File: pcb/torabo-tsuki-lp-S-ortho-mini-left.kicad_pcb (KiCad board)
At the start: 2 copper layers, 138.8 x 74 mm, 72 parts, among them J101 Conn_01x06_MountingPin, SW10 SW_Push, SW101 SW_SPDT, SW11 SW_Push, SW12 SW_Push, SW13 SW_Push, SW15 SW_Push, SW16 SW_Push, SW17 SW_Push, SW18 SW_Push, SW19 SW_Push, SW20 SW_Push, SW22 SW_Push, SW23 SW_Push, SW24 SW_Push, SW25 SW_Push, SW26 SW_Push, SW27 SW_Push, SW28 SW_Push, SW29 SW_Push, SW30 SW_Push, SW31 SW_Push, SW32 SW_Push, SW33 SW_Push, SW34 SW_Push, SW35 SW_Push, SW8 SW_Push, SW9 SW_Push, U101 XIAO nRF52840 Plus, U102 XCL103D503CR-G, U103 XC8111AA01MR-G

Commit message: Rename PCB silkscreen to kb-1
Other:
- board text added: "kb-1"
- board text removed: "torabo-tsuki om(s) v0"
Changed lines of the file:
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@@
 		)
 	)
-	(gr_text "torabo-tsuki om(s) v0"
+	(gr_text "kb-1"
 		(at 114 75.8 0)
 		(layer "F.SilkS")

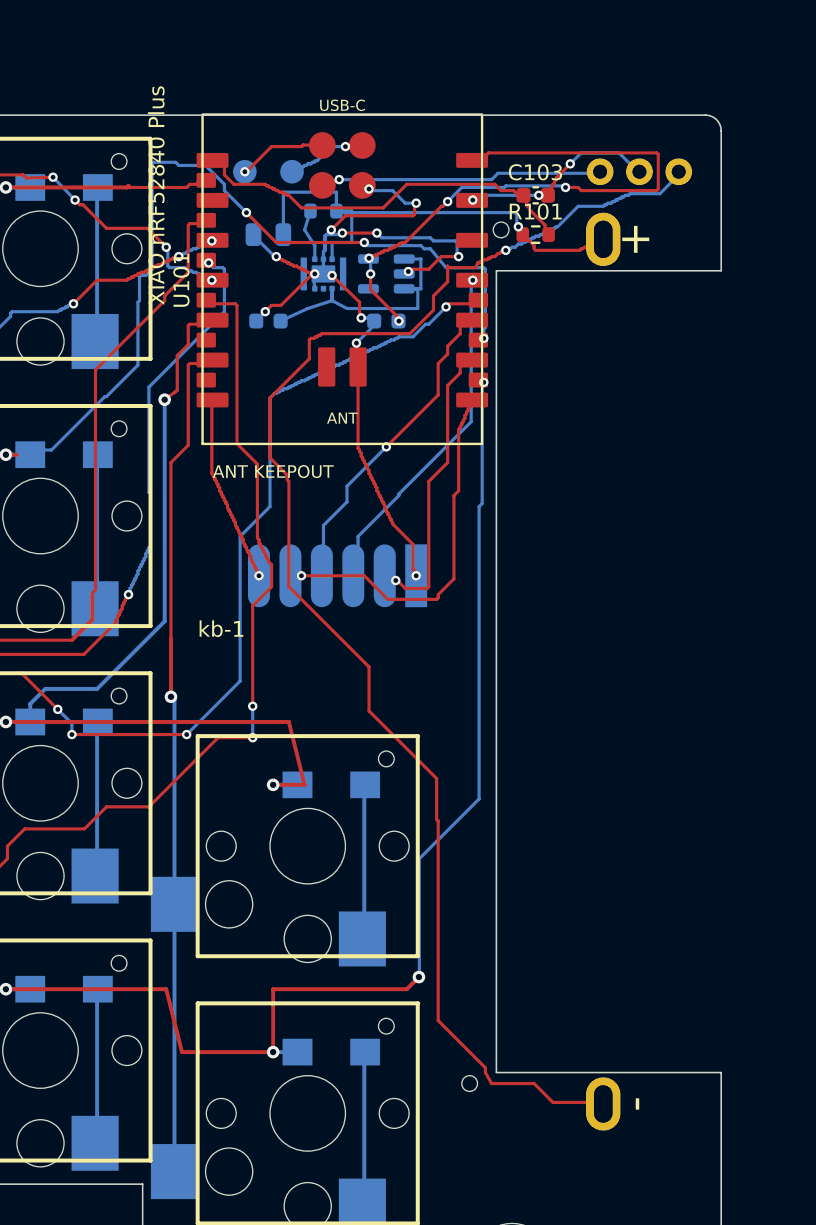
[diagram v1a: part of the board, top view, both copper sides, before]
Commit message: WIP: checkpoint single-XIAO PCB and vertical PHD conversion
Preserve the current single-controller PCB, schematics, documentation, and manufacturing artifacts. Include the vertical PHD placement/routing experiment; its candidate boards still fail DRC and are not production-ready.
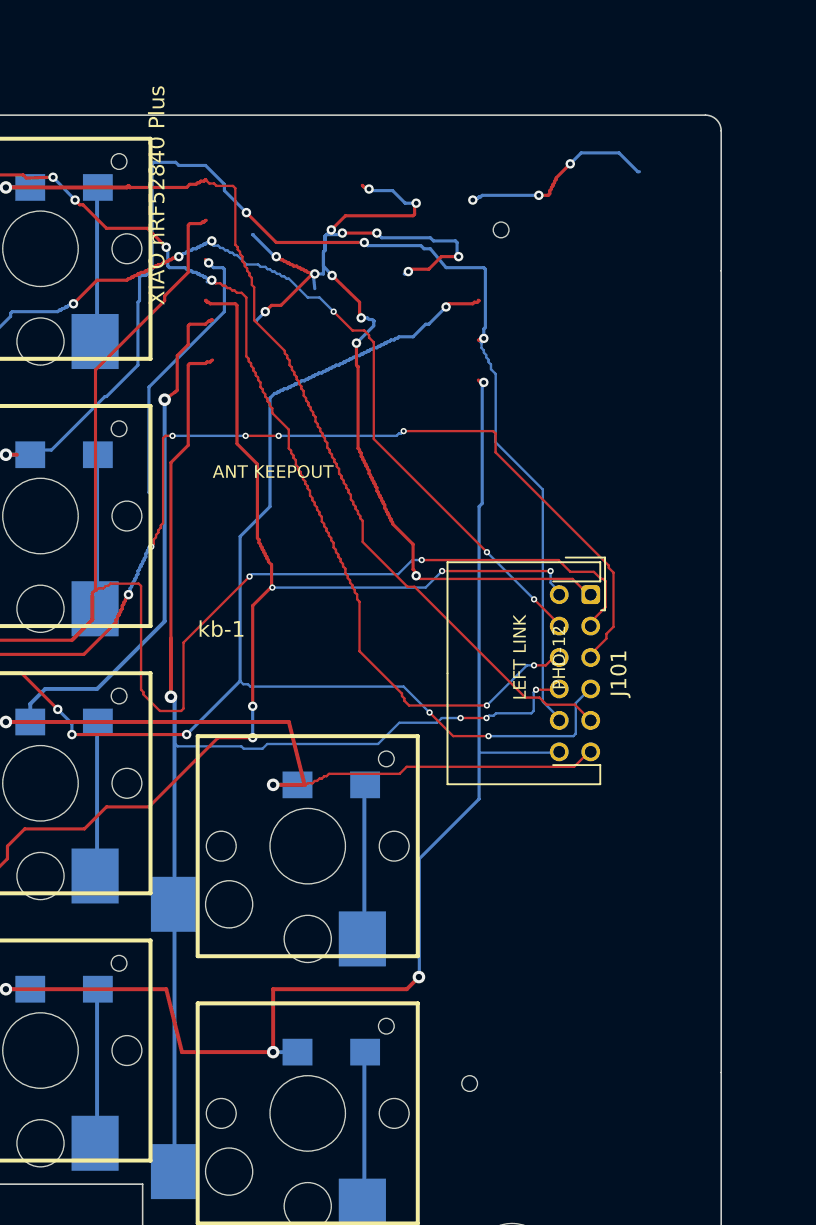
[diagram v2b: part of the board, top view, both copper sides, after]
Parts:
- removed BT101: GB-BH-4X1-WP, Library:battery_holder_AAA_1x_P55mm
- removed C101: 10uF 25V X5R, C_0805_2012Metric
- removed C102: 10uF 16V X5R, C_0603_1608Metric
- removed C103, C104: 0.1uF 50V X7R, C_0603_1608Metric
- removed R101: 10k, R_0603_1608Metric
- removed R102: 100k, R_0603_1608Metric
- removed SW101: SW_SPDT, Library:ISH-1260-HA-G
- removed TP101: SWDIO, TestPoint_Pad_D1.5mm
- removed TP102: SWDCLK, TestPoint_Pad_D1.5mm
- removed U101: XIAO nRF52840 Plus, XIAO-nRF52840-Plus-SMD
- removed U102: XCL103D503CR-G, CL-2025-02
- removed U103: XC8111AA01MR-G, SOT-23-5
- J101: value Conn_01x06_MountingPin -> S12B-PHDSS; footprint Library:ffc-6p-adapter -> Connector_JST:JST_PHD_S12B-PHDSS_2x06_P2.00mm_Horizontal; moved to F.Cu
- moved J101 16.1 mm to (139.0, 73.0), turned to -90 degrees
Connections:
- D10 pad 2: /left/ROW1 -> /left/LROW0
- D11 pad 2: /left/ROW1 -> /left/LROW0
- D12 pad 2: /left/ROW1 -> /left/LROW0
- D13 pad 2: /left/ROW1 -> /left/LROW0
- D15 pad 2: /left/ROW2 -> /left/LROW1
- D16 pad 2: /left/ROW2 -> /left/LROW1
- D17 pad 2: /left/ROW2 -> /left/LROW1
- D18 pad 2: /left/ROW2 -> /left/LROW1
- D19 pad 2: /left/ROW2 -> /left/LROW1
- D20 pad 2: /left/ROW2 -> /left/LROW1
- D22 pad 2: /left/ROW3 -> /left/LROW2
- D23 pad 2: /left/ROW3 -> /left/LROW2
- D24 pad 2: /left/ROW3 -> /left/LROW2
- D25 pad 2: /left/ROW3 -> /left/LROW2
- D26 pad 2: /left/ROW3 -> /left/LROW2
- D27 pad 2: /left/ROW3 -> /left/LROW2
- D28 pad 2: /left/ROW3 -> /left/LROW2
- D29 pad 2: /left/ROW4 -> /left/LROW3
- D30 pad 2: /left/ROW4 -> /left/LROW3
- D31 pad 2: /left/ROW4 -> /left/LROW3
- D32 pad 2: /left/ROW4 -> /left/LROW3
- D33 pad 2: /left/ROW4 -> /left/LROW3
- D34 pad 2: /left/ROW4 -> /left/LROW3
- D35 pad 2: /left/ROW4 -> /left/LROW3
- D8 pad 2: /left/ROW1 -> /left/LROW0
- D9 pad 2: /left/ROW1 -> /left/LROW0
- J101 pad 2: /left/SCLK -> /left/COL0
- J101 pad 3: /left/SDIO -> /left/COL1
- J101 pad 4: /left/MOTION -> /left/COL2
- J101 pad 5: /left/CS -> /left/COL3
- J101 pad 6: VCC -> /left/COL4
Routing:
- net /left/LROW3: track 0.00 -> 180.3 mm, vias 0 -> 9
- net /left/LROW1: track 0.00 -> 178.8 mm, vias 0 -> 9
- net /left/LROW2: track 0.00 -> 177.8 mm, vias 0 -> 8
- net /left/ROW4: track 175.1 -> 0.00 mm, vias 9 -> 0
- net /left/LROW0: track 0.00 -> 160.2 mm, vias 0 -> 6
- net /left/ROW3: track 158.7 -> 0.00 mm, vias 8 -> 0
- net /left/ROW2: track 152.4 -> 0.00 mm, vias 9 -> 0
- net /left/ROW1: track 113.0 -> 0.00 mm, vias 6 -> 0
- net Net-(BT101--): track 91.1 -> 0.00 mm, vias 1 -> 0
- net /left/COL1: track 170.8 -> 221.0 mm, vias 1 -> 3
- net /left/COL3: track 128.6 -> 175.3 mm, vias 3 -> 8
- net /left/COL4: track 97.3 -> 141.0 mm, vias 6 -> 8
- net /left/SYS_5V: track 39.7 -> 0.00 mm, vias 5 -> 0
- net /left/COL2: track 134.9 -> 171.0 mm, vias 5 -> 8
- net +BATT: track 31.6 -> 0.00 mm, vias 1 -> 0
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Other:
- outline, holes or cut-outs redrawn
- board text added: "LEFT LINK"
- board text added: "PHD-12"

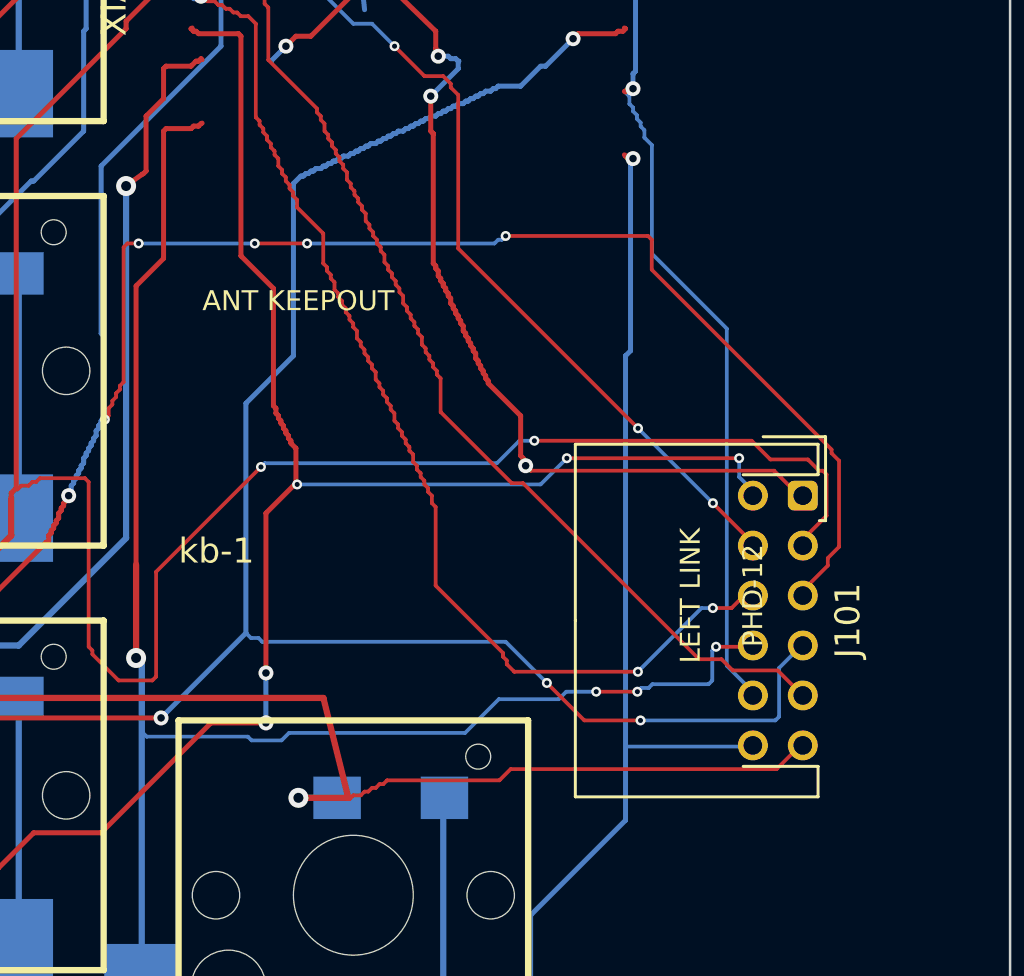
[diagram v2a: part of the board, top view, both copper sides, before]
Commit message: Use vertical JST PHD connectors on split PCBs
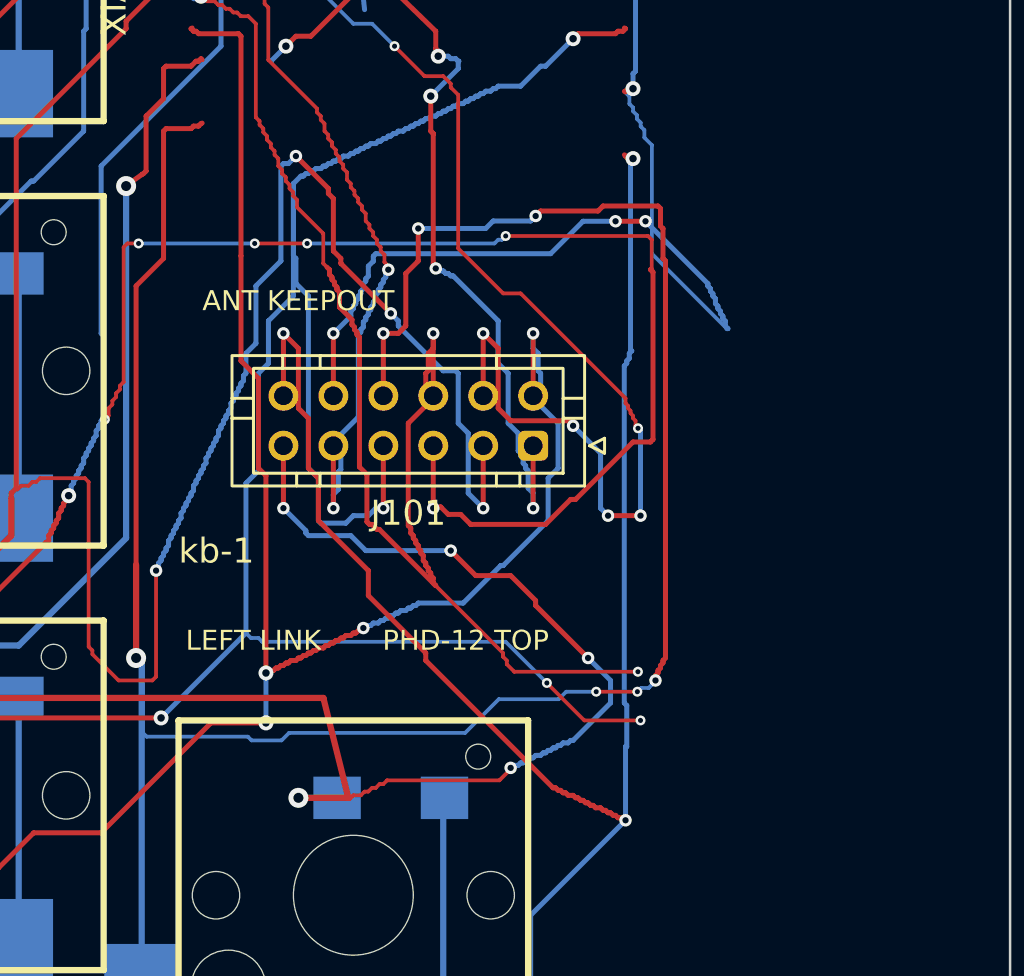
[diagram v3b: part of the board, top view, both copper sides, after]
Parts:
- J101: value S12B-PHDSS -> B12B-PHDSS; footprint Connector_JST:JST_PHD_S12B-PHDSS_2x06_P2.00mm_Horizontal -> Connector_JST:JST_PHD_B12B-PHDSS_2x06_P2.00mm_Vertical
- moved J101 11.0 mm to (128.2, 71.0), turned to 180 degrees
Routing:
- net /left/COL6: track 83.3 -> 115.0 mm, vias 4 -> 7
- net /left/LROW3: track 180.3 -> 204.0 mm, vias 9 -> 11
- net /left/LROW0: track 160.2 -> 147.3 mm, vias 6 -> 8
- net /left/LROW2: track 177.8 -> 190.3 mm, vias 8 -> 12
- net /left/COL2: track 171.0 -> 182.8 mm, vias 8 -> 11
- net /left/COL5: track 153.7 -> 164.1 mm, vias 7 -> 8
- net /left/LROW1: track 178.8 -> 187.1 mm, vias 9 -> 12
- net /left/COL4: track 141.0 -> 148.7 mm
- net GND: track 88.9 -> 81.7 mm, vias 17 -> 18
- net /left/COL1: track 221.0 -> 227.2 mm, vias 3 -> 5
- net /left/COL0: track 256.1 -> 259.5 mm, vias 10 -> 9
- net /left/COL3: track 175.3 -> 178.4 mm, vias 8 -> 9
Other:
- board text added: "PHD-12 TOP"
- board text removed: "PHD-12"

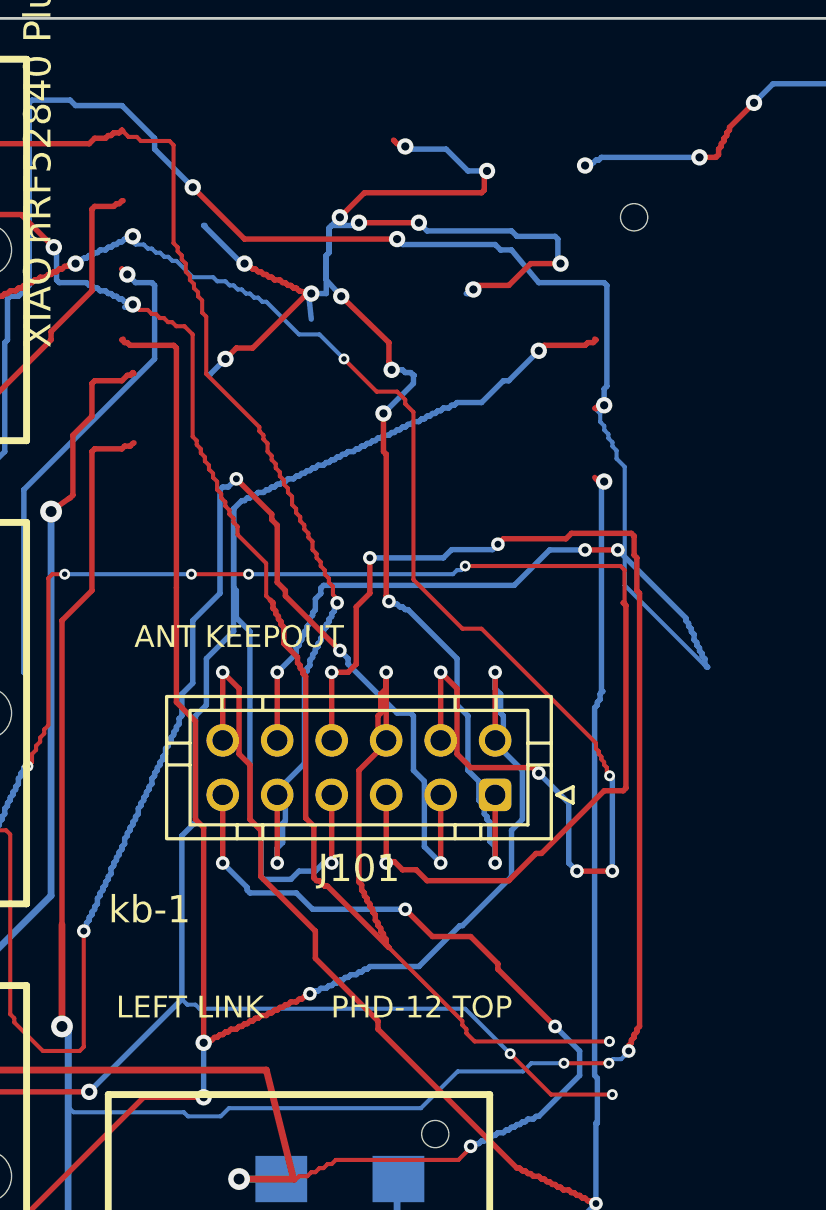
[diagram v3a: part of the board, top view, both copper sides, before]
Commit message: Replace split connectors with Samtec FFSD-compatible headers
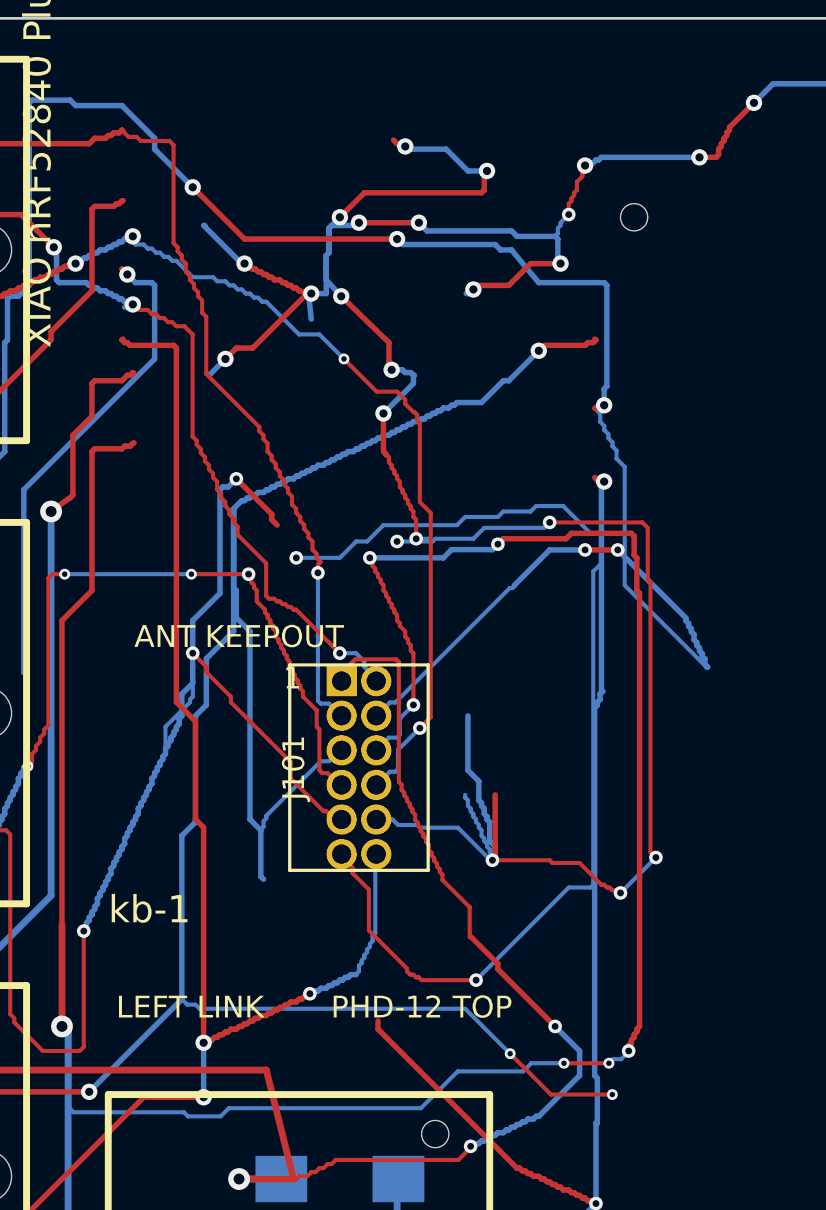
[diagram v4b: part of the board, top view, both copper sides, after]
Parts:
- J101: value B12B-PHDSS -> FTSH-106-01-L-D-K; footprint Connector_JST:JST_PHD_B12B-PHDSS_2x06_P2.00mm_Vertical -> Library:Samtec_FTSH-106-01-L-D-K
- moved J101 7.01 mm to (122.6, 66.8), turned to 0 degrees
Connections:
- J101 pad 1: GND -> /left/LROW2
- J101 pad 10: /left/LROW1 -> GND
- J101 pad 11: /left/LROW2 -> /left/LROW3
- J101 pad 12: /left/LROW3 -> /left/COL0
- J101 pad 2: /left/COL0 -> /left/COL4
- J101 pad 3: /left/COL1 -> /left/LROW0
- J101 pad 4: /left/COL2 -> /left/LROW1
- J101 pad 5: /left/COL3 -> /left/COL5
- J101 pad 6: /left/COL4 -> /left/COL6
- J101 pad 7: /left/COL5 -> /left/COL3
- J101 pad 8: /left/COL6 -> /left/COL2
- J101 pad 9: /left/LROW0 -> /left/COL1
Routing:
- net GND: track 81.7 -> 114.6 mm, vias 18 -> 23
- net /left/COL4: track 148.7 -> 116.1 mm, vias 8 -> 7
- net /left/COL3: track 178.4 -> 152.6 mm, vias 9 -> 7
- net /left/LROW3: track 204.0 -> 225.4 mm, vias 11 -> 12
- net /left/COL2: track 182.8 -> 162.9 mm, vias 11 -> 7
- net /left/COL0: track 259.5 -> 246.5 mm, vias 9 -> 8
- net /left/LROW0: track 147.3 -> 138.8 mm, vias 8 -> 7
- net /left/LROW1: track 187.1 -> 180.8 mm, vias 12 -> 11
- net /left/COL1: track 227.2 -> 222.3 mm, vias 5 -> 4
- net /left/LROW2: track 190.3 -> 191.4 mm, vias 12 -> 10
- net /left/COL6: track 115.0 -> 115.8 mm
- net /left/COL5: track 164.1 -> 163.3 mm, vias 8 -> 7
